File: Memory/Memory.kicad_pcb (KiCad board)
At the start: 2 copper layers, 100 x 100 mm, 13 parts, among them U1 62256, U2 6264, U3 6264, U4 28C64, U5 74LS139

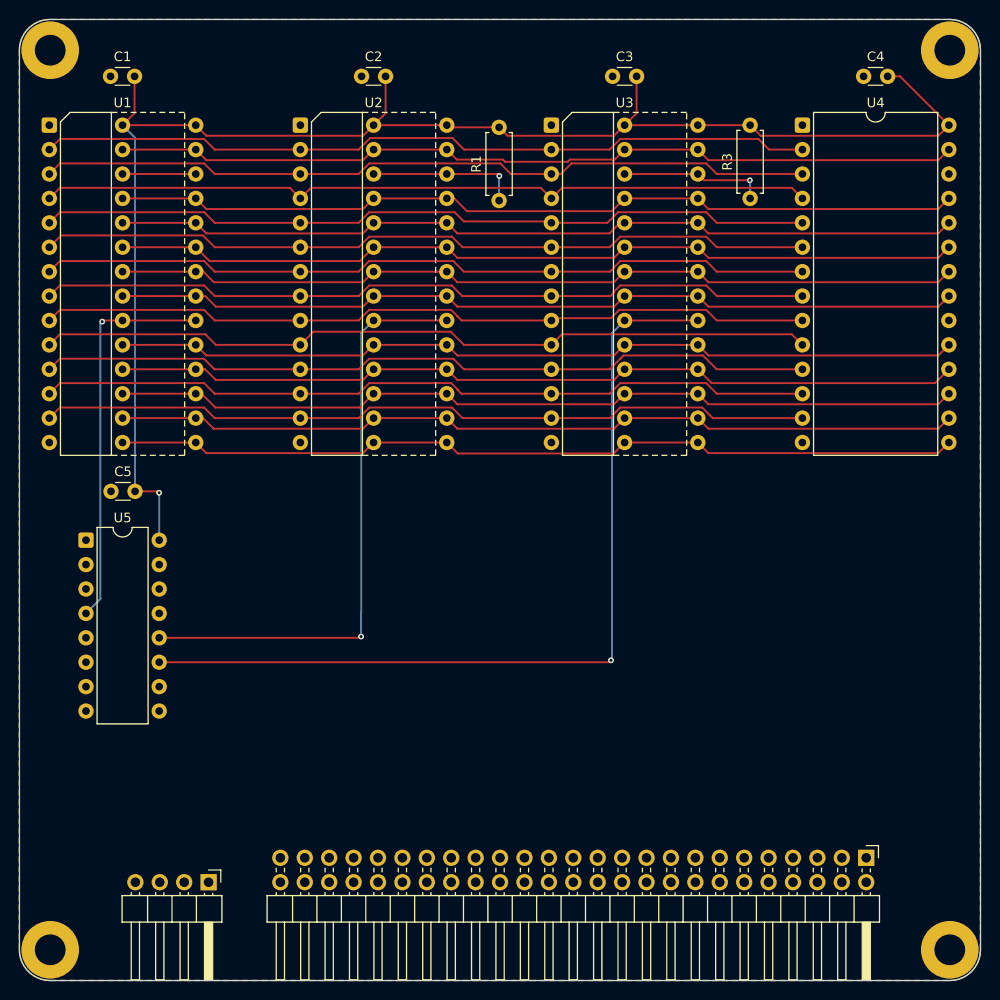
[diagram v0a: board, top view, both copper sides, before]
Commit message: outputs to terminal/log file
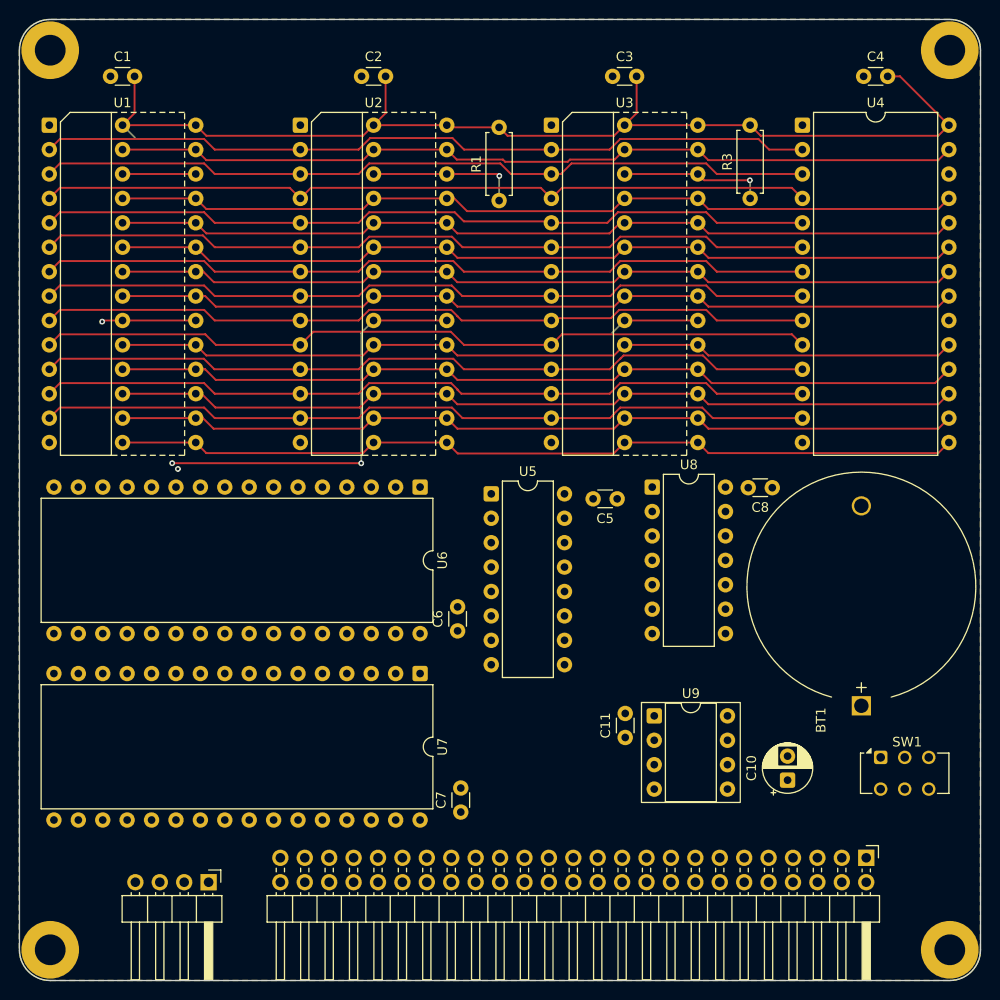
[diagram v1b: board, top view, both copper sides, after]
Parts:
- added BT1: CR2032, Battery:BatteryHolder_MYOUNG_BS-07-A1BJ001_CR2032, F.Cu at (112.6, 96.4)
- added C10: 10µF, Capacitor_THT:CP_Radial_D5.0mm_P2.50mm, F.Cu at (104.9, 104.2)
- added C11: 100n, Capacitor_THT:C_Disc_D3.0mm_W1.6mm_P2.50mm, F.Cu at (88.0, 99.7)
- added C6: 100n, Capacitor_THT:C_Disc_D3.0mm_W1.6mm_P2.50mm, F.Cu at (70.6, 88.6)
- added C7: 100n, Capacitor_THT:C_Disc_D3.0mm_W1.6mm_P2.50mm, F.Cu at (70.9, 107.5)
- added C8: 100n, Capacitor_THT:C_Disc_D3.0mm_W1.6mm_P2.50mm, F.Cu at (103.3, 73.7)
- added SW1: Battery, Button_Switch_THT:SW_CK_JS202011CQN_DPDT_Straight, F.Cu at (114.6, 101.8)
- added U6: AS6C4008-55PCN, Package_DIP:DIP-32_W15.24mm, F.Cu at (66.7, 73.7)
- added U7: AS6C4008-55PCN, Package_DIP:DIP-32_W15.24mm, F.Cu at (66.7, 93.1)
- added U8: 74HCT00, Package_DIP:DIP-14_W7.62mm, F.Cu at (90.8, 73.7)
- added U9: DS1210, Package_DIP:DIP-8_W7.62mm_Socket, F.Cu at (91.0, 97.5)
- moved C5 52.7 mm to (87.2, 74.9), turned to 180 degrees
- moved U5 42.4 mm to (74.1, 74.4)
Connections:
- BRD1 pad 10: unconnected-(BRD1D-S5-Pad10) -> BANK0
- BRD1 pad 12: unconnected-(BRD1D-S6-Pad12) -> BANK1
- BRD1 pad 14: DBE -> BANK2
- BRD1 pad 16: BA -> BANK3
- BRD1 pad 18: VMA -> BANK4
- BRD1 pad 2: unconnected-(BRD1D-S1-Pad2) -> ~{RAM_CS}
- BRD1 pad 20: unconnected-(BRD1D-S10-Pad20) -> BANK5
- BRD1 pad 32: (no net) -> unconnected-(BRD1-Pad32)
- BRD1 pad 33: R/~{W} -> unconnected-(BRD1-BUS_OK-Pad33)
- BRD1 pad 34: (no net) -> unconnected-(BRD1-Pad34)
- BRD1 pad 36: ~{HALT} -> unconnected-(BRD1-Pad36)
- BRD1 pad 38: (no net) -> unconnected-(BRD1-Pad38)
- BRD1 pad 4: unconnected-(BRD1D-S2-Pad4) -> ~{ROM_CS}
- BRD1 pad 40: (no net) -> unconnected-(BRD1-Pad40)
- BRD1 pad 42: (no net) -> unconnected-(BRD1-Pad42)
- BRD1 pad 44: (no net) -> unconnected-(BRD1-Pad44)
- BRD1 pad 46: (no net) -> R/~{W}
- BRD1 pad 48: (no net) -> ~{IRQ}
- BRD1 pad 50: (no net) -> ~{RESET}
- BRD1 pad 6: unconnected-(BRD1D-S3-Pad6) -> ~{BANK_CS}
- BRD1 pad VCC: +5V -> (no net)
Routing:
- net ~{RAM_{H1}_CS}: track 90.7 -> 9.56 mm
- net +5V: track 160.1 -> 115.8 mm, vias 1 -> 0
- net ~{RAM_{L}_CS}: track 40.8 -> 10.0 mm
- net ~{RAM_{H0}_CS}: track 62.1 -> 42.7 mm, vias 1 -> 2

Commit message: a bunch of stuff
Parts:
- removed BT1: CR2032, Battery:BatteryHolder_MYOUNG_BS-07-A1BJ001_CR2032
- removed C10: 10µF, Capacitor_THT:CP_Radial_D5.0mm_P2.50mm
- removed C11, C6, C7, C8: 100n, Capacitor_THT:C_Disc_D3.0mm_W1.6mm_P2.50mm
- removed SW1: Battery, Button_Switch_THT:SW_CK_JS202011CQN_DPDT_Straight
- removed U6, U7: AS6C4008-55PCN, Package_DIP:DIP-32_W15.24mm
- removed U8: 74HCT00, Package_DIP:DIP-14_W7.62mm
- removed U9: DS1210, Package_DIP:DIP-8_W7.62mm_Socket
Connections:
- BRD1 pad 10: BANK0 -> unconnected-(BRD1-BANK_{0}-Pad10)
- BRD1 pad 12: BANK1 -> unconnected-(BRD1-BANK_{1}-Pad12)
- BRD1 pad 14: BANK2 -> unconnected-(BRD1-BANK_{2}-Pad14)
- BRD1 pad 16: BANK3 -> unconnected-(BRD1-BANK_{3}-Pad16)
- BRD1 pad 18: BANK4 -> unconnected-(BRD1-BANK_{4}-Pad18)
- BRD1 pad 20: BANK5 -> unconnected-(BRD1-BANK_{5}-Pad20)

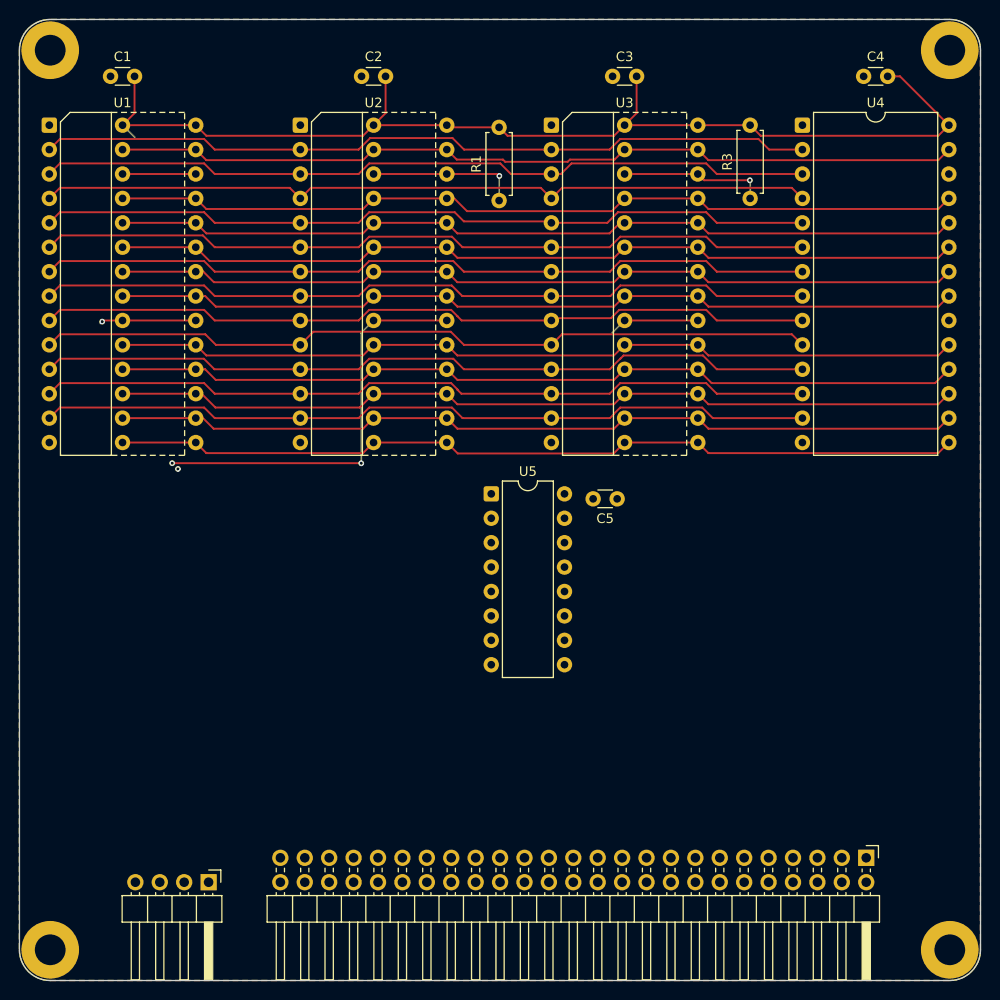
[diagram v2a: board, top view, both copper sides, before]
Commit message: ordered memory board
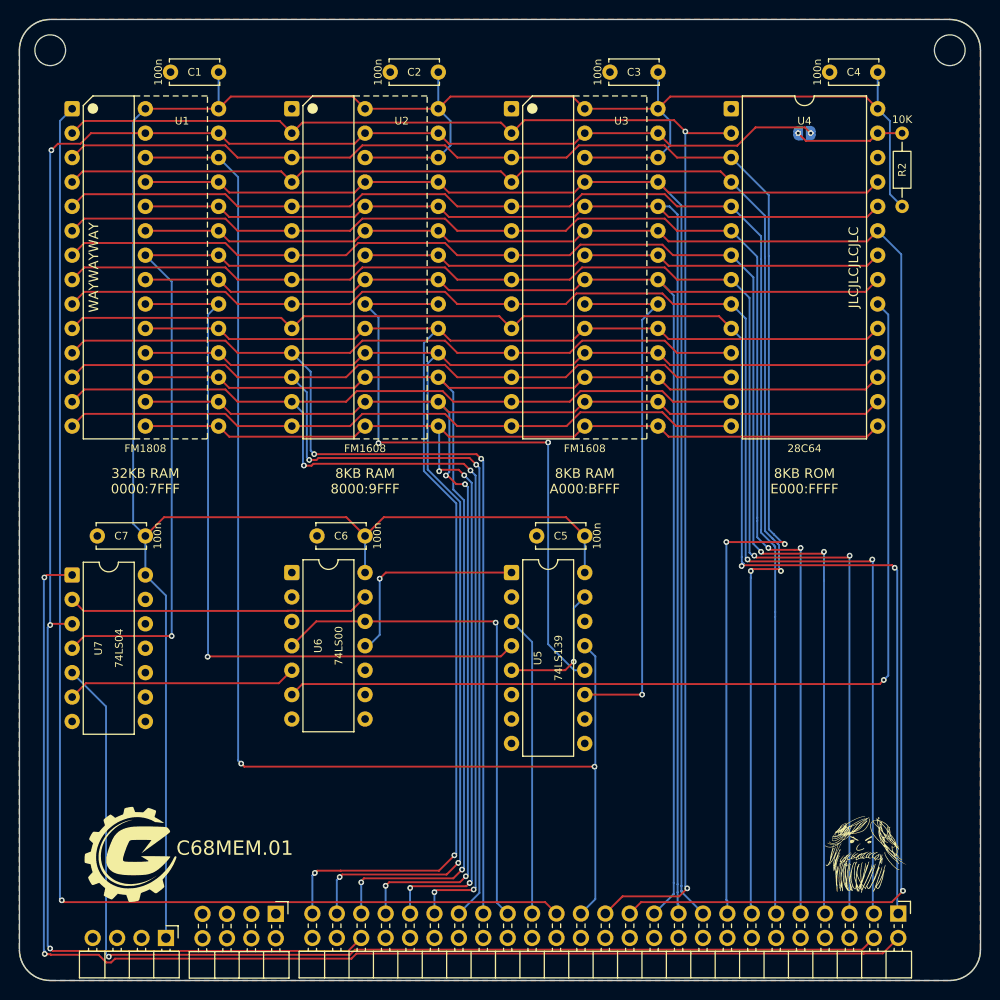
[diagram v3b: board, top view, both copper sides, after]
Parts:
- removed BRD1: Card, 0-Footprints:Card
- removed R1, R3: 1K, Resistor_THT:R_Axial_DIN0207_L6.3mm_D2.5mm_P7.62mm_Horizontal
- added C6: 100n, 0-Footprints:C_Disc_D5.0mm_W2.5mm_P5.00mm, F.Cu at (56.0, 78.7)
- added C7: 100n, 0-Footprints:C_Disc_D5.0mm_W2.5mm_P5.00mm, F.Cu at (33.1, 78.7)
- added G1: Logo, 0-Footprints:Crank, F.Cu at (36.6, 111.9)
- added G2: Logo, 0-Footprints:crankery_small, F.Cu at (112.7, 112.0)
- added J1: Buss, 0-Footprints:Card, F.Cu at (25.0, 25.0)
- added JP1: ROM_WE, 0-Footprints:SolderJumper-2_P1.3mm_Open_RoundedPad1.0x1.5mm, B.Cu at (106.7, 36.8)
- added R2: 10K, 0-Footprints:R_Axial_DIN0204_L3.6mm_D1.6mm_P7.62mm_Horizontal, F.Cu at (116.8, 44.5)
- added U6: 74LS00, 0-Footprints:DIP-14_W7.62mm, F.Cu at (53.3, 82.5)
- added U7: 74LS04, 0-Footprints:DIP-14_W7.62mm, F.Cu at (30.5, 82.8)
- C1, C2, C3, C4, C5: footprint Capacitor_THT:C_Disc_D3.0mm_W1.6mm_P2.50mm -> 0-Footprints:C_Disc_D5.0mm_W2.5mm_P5.00mm
- U1: value 62256 -> FM1808
- U2, U3: value 6264 -> FM1608
- U4: footprint Package_DIP:DIP-28_W15.24mm -> 0-Footprints:DIP-28_W15.24mm
- U5: footprint Package_DIP:DIP-16_W7.62mm -> 0-Footprints:DIP-16_W7.62mm
- moved C1 11.3 mm to (45.7, 30.5), turned to 180 degrees
- moved C5 9.22 mm to (78.8, 78.7), turned to 0 degrees
- moved U5 8.46 mm to (76.2, 82.5)
- moved C2 8.00 mm to (68.6, 30.5), turned to 180 degrees
- moved U4 7.60 mm to (99.1, 34.3)
- moved C3 4.75 mm to (91.4, 30.5), turned to 180 degrees
- moved U3 4.48 mm to (76.2, 34.3)
- moved U1 2.93 mm to (30.5, 34.3)
- moved U2 1.93 mm to (53.3, 34.3)
- moved C4 1.53 mm to (114.3, 30.5), turned to 180 degrees
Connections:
- net ~{RAM_{H0}_CS} renamed ~{RAM_{H0}_CS_RDY}
- net ~{RAM_{H1}_CS} renamed ~{RAM_{H1}_CS_RDY}
- net ~{RAM_{L}_CS} renamed ~{RAM_{L}_CS_RDY}
- C1 pad 1: GND -> +5V
- C1 pad 2: +5V -> GND
- C2 pad 1: GND -> +5V
- C2 pad 2: +5V -> GND
- C3 pad 1: GND -> +5V
- C3 pad 2: +5V -> GND
- C4 pad 1: GND -> +5V
- C4 pad 2: +5V -> GND
- U2 pad 26: Net-(U2-CS2) -> +5V
- U3 pad 26: Net-(U3-CS2) -> +5V
- U4 pad 20: ~{ROM_CS} -> ~{ROM_CS_RDY}
- U4 pad 27: R/~{W} -> Net-(JP1-B)
- U5 pad 1: ~{RAM_CS} -> Net-(U5A-E)
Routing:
- net +5V: track 115.8 -> 278.1 mm
- net A14: track 0.00 -> 135.0 mm, vias 0 -> 1
- net ~{RAM_CS}: track 0.00 -> 132.5 mm, vias 0 -> 2
- net A13: track 7.62 -> 137.5 mm, vias 0 -> 2
- net R/~{W}: track 88.9 -> 201.8 mm, vias 0 -> 4
- net ~{ROM_CS}: track 0.00 -> 111.6 mm, vias 0 -> 1
- net ~{ROM_CS_RDY}: track 0.00 -> 102.0 mm, vias 0 -> 1
- net A11: track 89.0 -> 178.1 mm, vias 0 -> 1
- net A12: track 81.2 -> 160.1 mm, vias 0 -> 2
- net A7: track 81.1 -> 159.2 mm, vias 0 -> 2
- net GND: track 0.00 -> 71.9 mm
- net A6: track 81.1 -> 152.9 mm, vias 0 -> 2
- net A8: track 88.9 -> 157.0 mm
- net A1: track 81.1 -> 149.1 mm, vias 0 -> 2
- net A2: track 81.1 -> 149.0 mm, vias 0 -> 2
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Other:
- board text added: "32KB RAM 0000:7FFF"
- board text added: "8KB RAM 8000:9FFF"
- board text added: "8KB RAM A000:BFFF"
- board text added: "8KB ROM E000:FFFF"
- board text added: "C68MEM.01"
- board text added: "Crankery - April 2026 - Dave Hamilton"
- board text added: "JLCJLCJLCJLC"
- board text added: "WAYWAYWAY"

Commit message: finish routing the coms board. add some step models to look at this thing in freecad
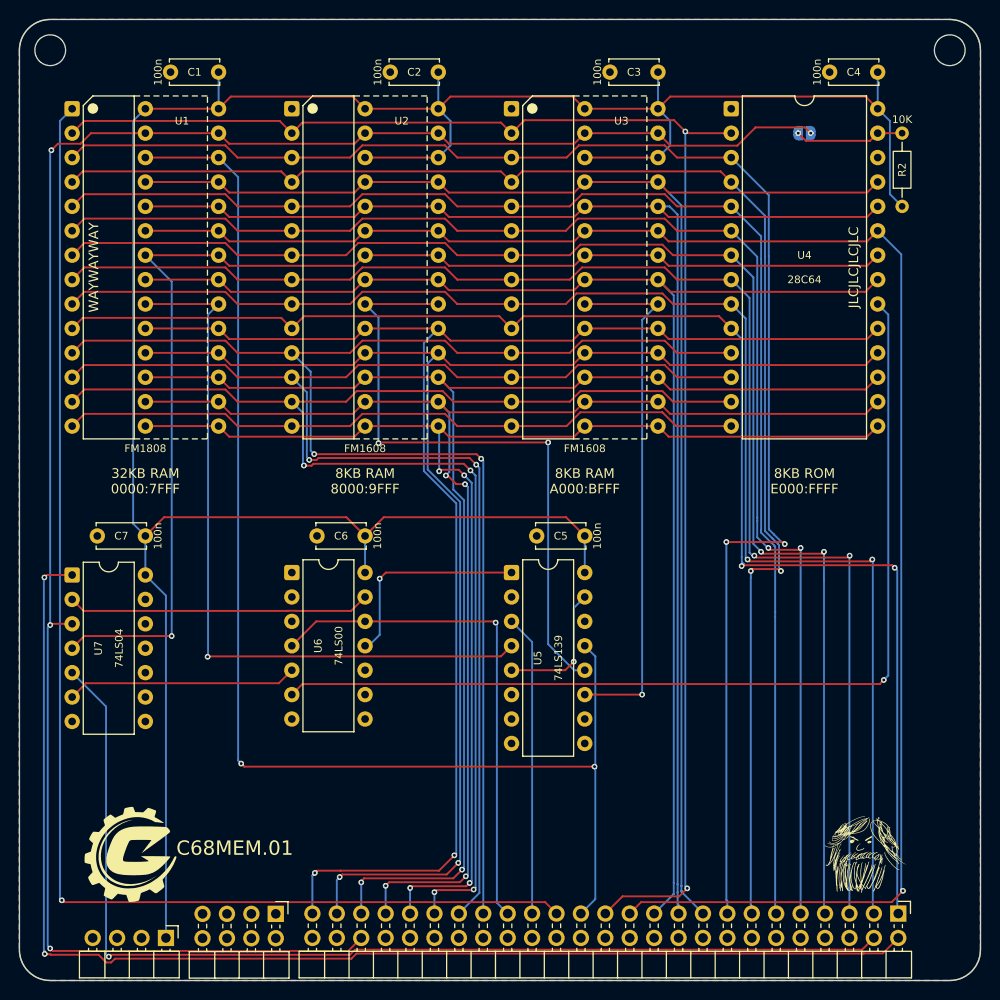
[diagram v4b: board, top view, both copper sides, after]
